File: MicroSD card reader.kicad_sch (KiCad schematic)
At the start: 17 parts, among them J3 MSD-3-A, U5 AMS1117-3.3, U8 74LVC125

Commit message: proba
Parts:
- J3: value MSD-3-A -> MSD-3-A MicroSD card socket
- U8: value 74LVC125 -> 74LVC125 Buffer
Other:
- note added: "MicroSD card Reader"
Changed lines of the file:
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@@
 	(generator_version "9.0")
 	(paper "A4")
+	(text "MicroSD card Reader"
+		(exclude_from_sim no)
+		(at 144.272 26.67 0)
+		(effects
+			(font
+				(size 5.08 5.08)
+				(thickness 1.016)
+				(bold yes)
+			)
+		)
+	)
 	(junction
 		(at 135.89 77.47)
@@
 			)
 		)
-		(property "Value" "MSD-3-A"
+		(property "Value" "MSD-3-A MicroSD card socket"
 			(at 222.25 113.6649 0)
 			(effects
@@
 			)
 		)
-		(property "Value" "74LVC125"
+		(property "Value" "74LVC125 Buffer"
 			(at 106.68 85.09 0)
 			(effects

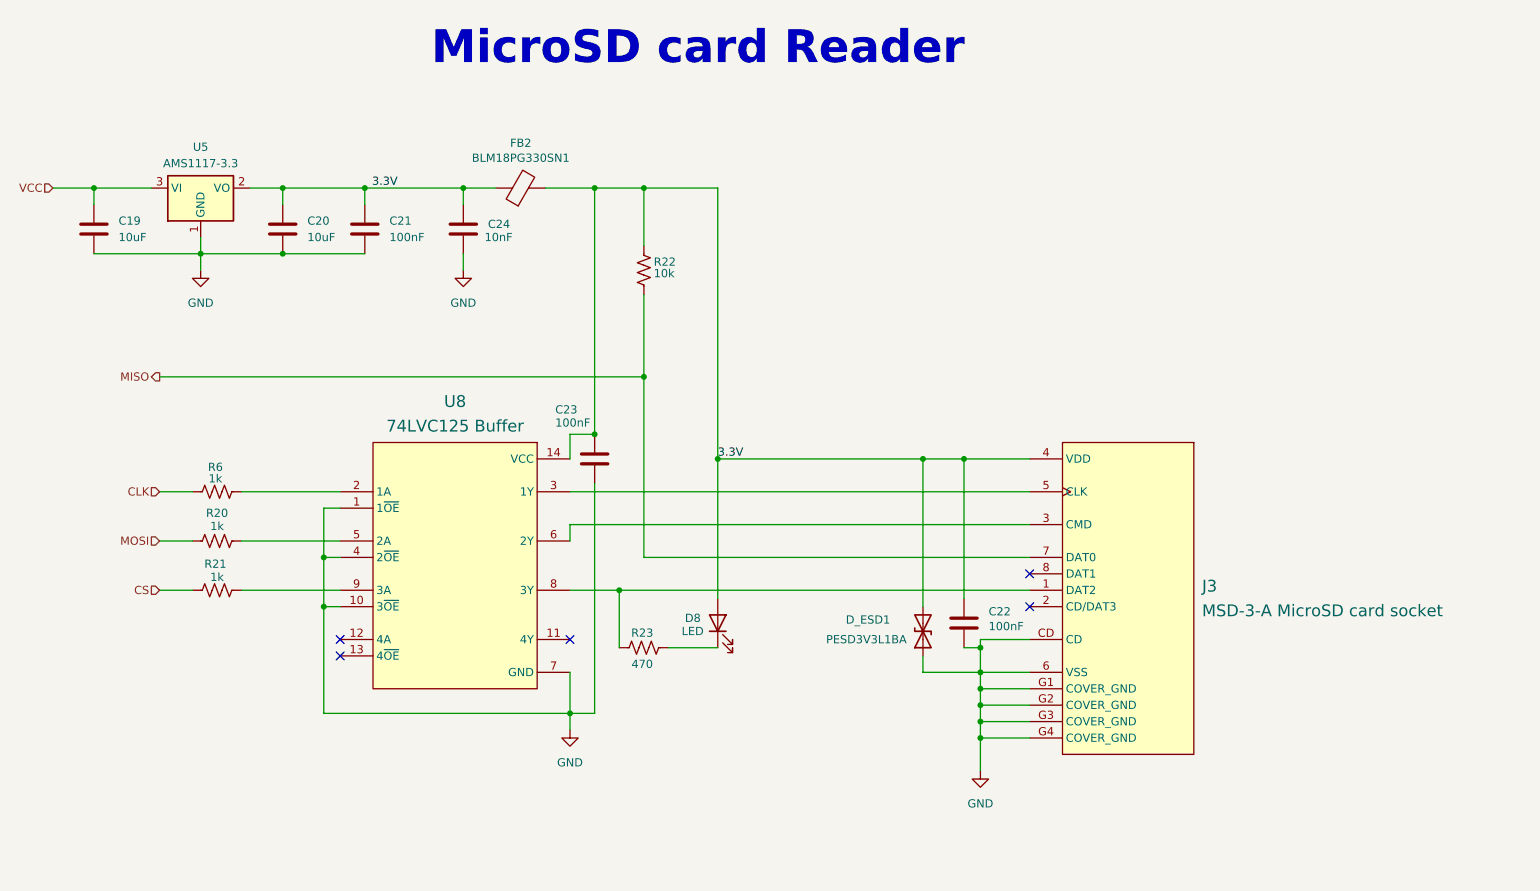
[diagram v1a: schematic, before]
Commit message: Zamena Buffer-a sa LevelShifter-om
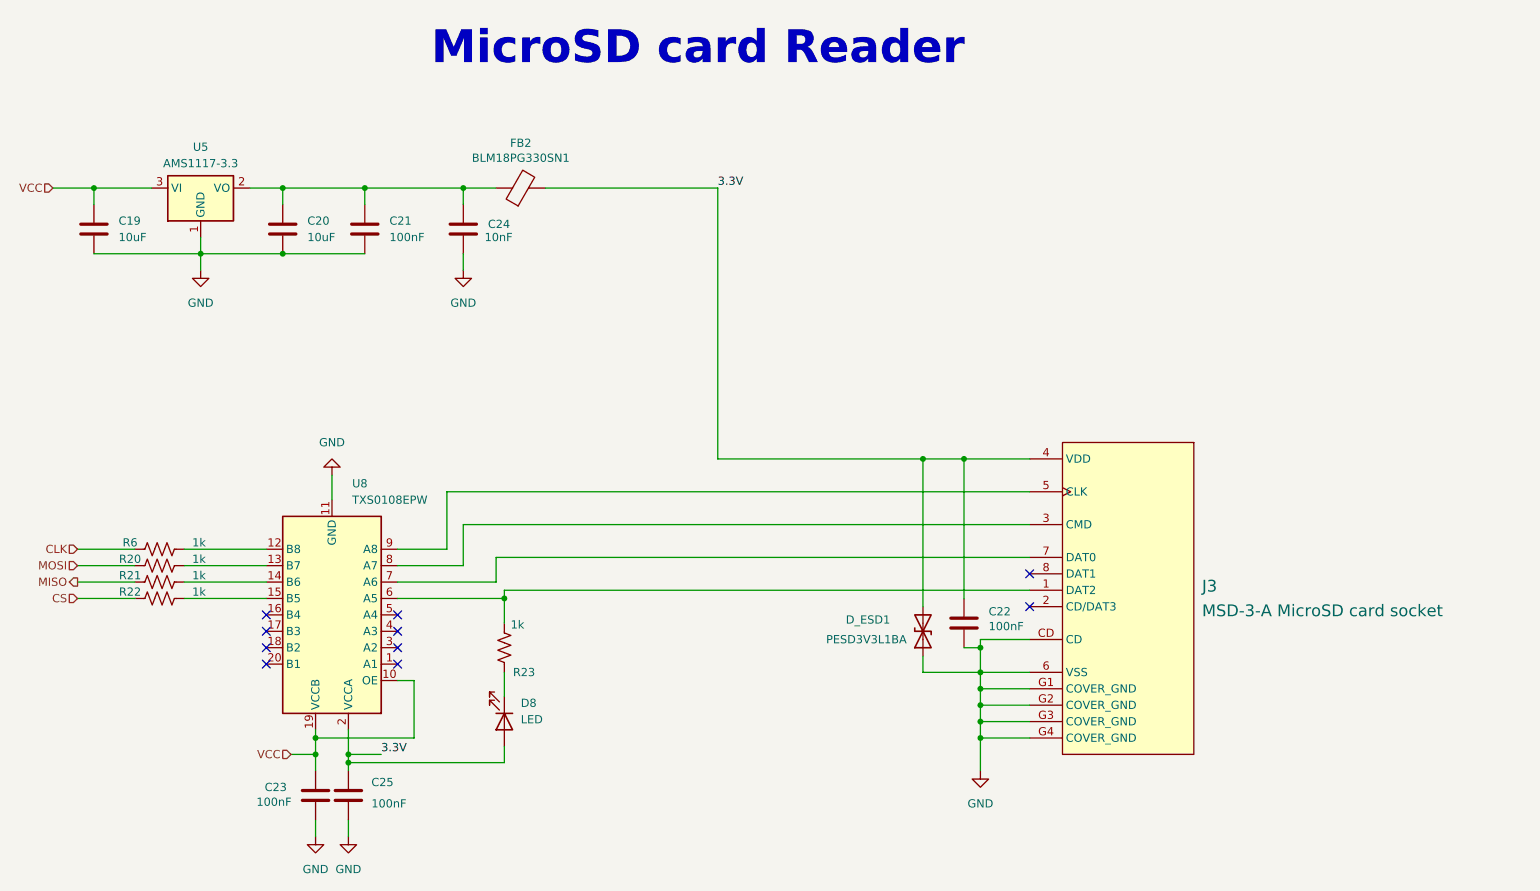
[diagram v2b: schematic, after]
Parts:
- removed U8: 74LVC125 Buffer, 74LVC125APW_118:IC_74LVC125APW,118, symbol 74LVC125APW_118:74LVC125APW,118
- added C25: 100nF, Capacitor_SMD:C_0805_2012Metric, symbol Device:C
- added U8: TXS0108EPW, Package_SO:TSSOP-20_4.4x6.5mm_P0.65mm, symbol Logic_LevelTranslator:TXS0108EPW
- R22: value 10k -> 1k
- R23: value 470 -> 1k
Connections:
- net 3.3V: now also C25.1, U8.2 (VCCA); no longer C20.1, C21.1, C23.1, C24.1, FB2.1, R22.2, U5.2 (VO)
- net CS: now also R22.1; no longer R21.1
- net GND: now also C25.2, U8.11 (GND)
- net MISO: now also R21.1; no longer J3.7 (DAT0), R22.1
- net VCC: now also C23.1, U8.10 (OE), U8.19 (VCCB)
- net at R21.2: now also U8.14 (B6)
- net at R23.2: now also J3.1 (DAT2), U8.6 (A5); no longer D8.1 (K)
- net at R20.2: now also U8.13 (B7)
- net at R23.1: now also D8.1 (K); no longer J3.1 (DAT2)
- net at J3.3 (CMD): now also U8.8 (A7)
- net at J3.5 (CLK): now also U8.9 (A8)
- net at R6.2: now also U8.12 (B8)
- new net: R22.2, U8.15 (B5)
- new net: J3.7 (DAT0), U8.7 (A6)
- new net: C20.1, C21.1, C24.1, FB2.1, U5.2 (VO)
- no-connect marks 5 -> 10
